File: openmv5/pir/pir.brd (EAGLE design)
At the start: 35.6 x 26.7 mm, 60 parts, among them IC1 AP3032KTR-G1, IC2 AP3032KTR-G1, J1 OPENMV5-TOP, Q1 2N7002KW_R1_00001, U1 EKMB1307113K, U2 MIC5365-3.3YMT-TZ

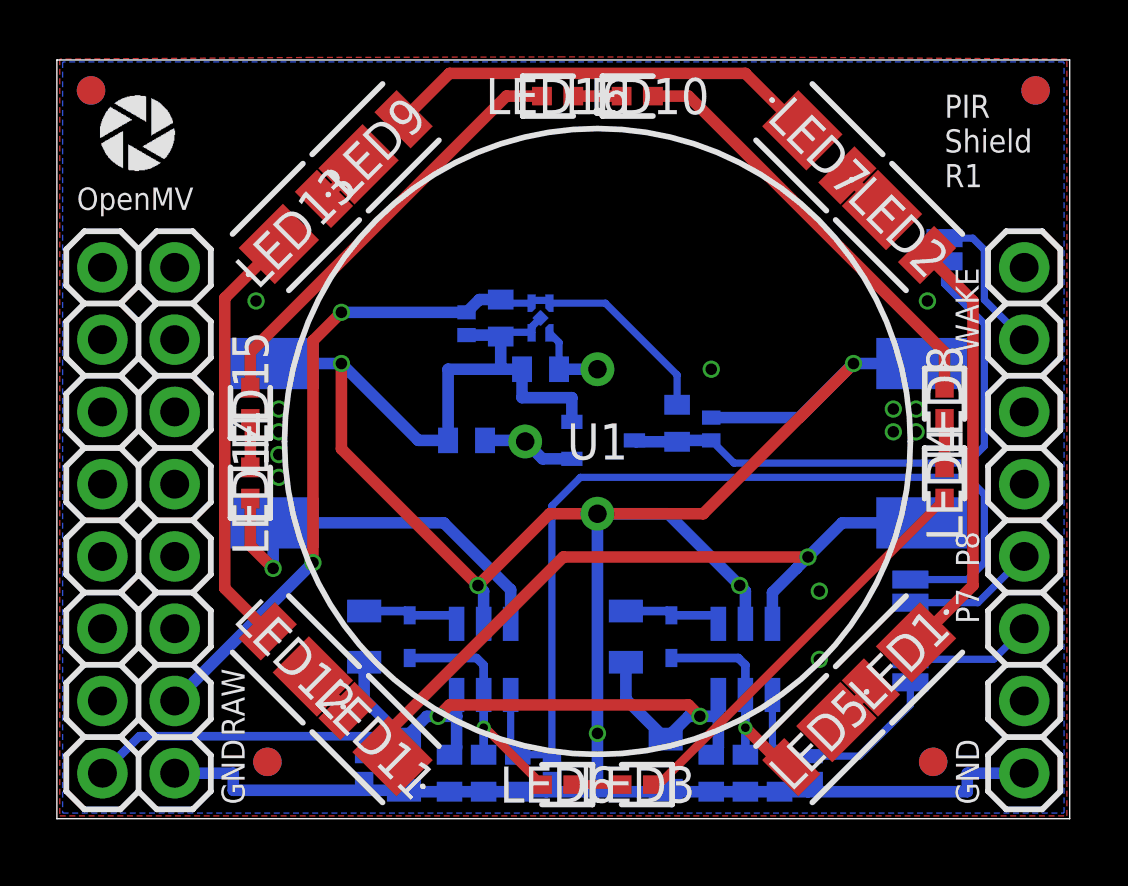
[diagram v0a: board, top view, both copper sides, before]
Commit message: Final PIR shield, fixed regulator
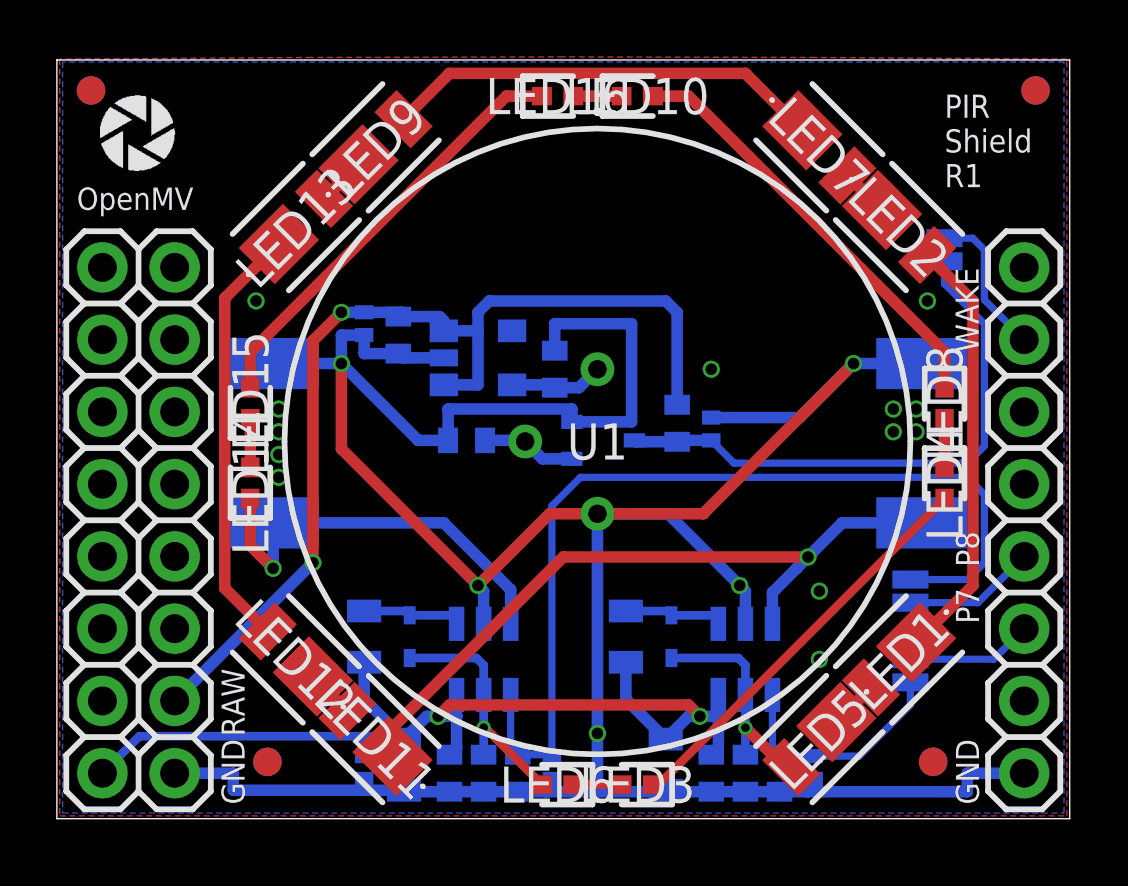
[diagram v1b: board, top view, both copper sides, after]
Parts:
- removed U2: MIC5365-3.3YMT-TZ, MIC5365-3.3YMT-TZ:VREG_MIC5365-3.3YMT-TZ
- added IC3: TCR2LF33,LM_CT, TCR2LF33_LM_CT:TCR2LF33LMCT
- moved C7 3.65 mm to (12.0, 17.0)
- moved D7 3.60 mm to (10.8, 17.4)
- moved C8 0.50 mm to (17.5, 15.8), turned to 270 degrees
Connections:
- net GND: now also IC3.2; no longer U2.2, U2.EP
- net RAW: now also IC3.1, IC3.3; no longer U2.3, U2.4
- net VDD: now also IC3.5; no longer U2.1
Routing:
- net GND: track 106.1 -> 113.9 mm
- net RAW: track 30.4 -> 36.2 mm
- net VDD: track 2.77 -> 3.31 mm

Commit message: Add more options
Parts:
- added JP4: JUMPER-SMT_2_NO_SILK, SparkFun-Jumpers:SMT-JUMPER_2_NO_SILK
- R5: value 1K -> 100K
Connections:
- new net P11_WAKEUP_INT_2: J1.13, JP4.1
- net P11_WAKEUP: now also JP4.2
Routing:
- net P11_WAKEUP_INT_2: track 0.00 -> 22.5 mm, vias 0 -> 2
- net GND: track 113.9 -> 115.0 mm
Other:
- board text added: "WAKE P11"
- board text added: "WAKE P9"
- board text removed: "WAKE"
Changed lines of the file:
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@@
 <wire x1="35.6" y1="26.67" x2="0" y2="26.67" width="0" layer="20"/>
 <wire x1="0" y1="26.67" x2="0" y2="0" width="0" layer="20"/>
-<text x="24.4" y="19" size="0.8128" layer="22" font="vector" ratio="20" rot="MR0">https://openmv.io</text>
+<text x="23.2" y="19" size="0.8128" layer="22" font="vector" ratio="20" rot="MR0">https://openmv.io</text>
 <text x="0.7" y="21.4" size="0.7874" layer="21" font="vector" ratio="20" distance="30">OpenMV</text>
-<text x="24.4" y="20.4" size="0.8128" layer="22" font="vector" ratio="20" rot="MR0">PIR Shield R1</text>
-<text x="24.4" y="17.6" size="0.8128" layer="22" font="vector" ratio="20" rot="MR0">3.31.23</text>
+<text x="23.2" y="20.4" size="0.8128" layer="22" font="vector" ratio="20" rot="MR0">PIR Shield R1</text>
+<text x="23.2" y="17.6" size="0.8128" layer="22" font="vector" ratio="20" rot="MR0">3.31.23</text>
 <text x="5.8" y="0.5" size="0.8128" layer="22" font="vector" ratio="22" rot="MR90">GND</text>
 <text x="32.4" y="2.8" size="0.8128" layer="22" font="vector" ratio="22" rot="MR270">GND</text>
@@
 <text x="6.6" y="2.9" size="0.8128" layer="21" font="vector" ratio="22" rot="R90">RAW</text>
 <text x="31.6" y="2.8" size="0.8128" layer="21" font="vector" ratio="22" rot="R270">GND</text>
-<text x="31.6" y="8.1" size="0.8128" layer="21" font="vector" ratio="22" rot="R270">P7</text>
-<text x="31.6" y="10.1" size="0.8128" layer="21" font="vector" ratio="22" rot="R270">P8</text>
-<text x="32.4" y="16.4" size="0.8128" layer="21" font="vector" ratio="22" rot="R90">WAKE</text>
 <text x="10.8" y="14" size="0.8128" layer="22" font="vector" ratio="20" rot="MR270">Hot</text>
 <text x="27.2" y="12" size="0.8128" layer="22" font="vector" ratio="20" rot="MR90">Hot</text>
 <text x="28.6" y="6" size="0.8128" layer="22" font="vector" ratio="22" rot="MR270">P7</text>
 <text x="28.6" y="8.8" size="0.8128" layer="22" font="vector" ratio="22" rot="MR270">P8</text>
-<text x="29.9" y="21.5" size="0.8128" layer="22" font="vector" ratio="22" rot="MR270">WAKE</text>
+<text x="29.9" y="21.5" size="0.8128" layer="22" font="vector" ratio="22" rot="MR270">WAKE
+P11</text>
 <text x="5.8" y="2.9" size="0.8128" layer="22" font="vector" ratio="22" rot="MR90">RAW</text>
+<text x="27.1" y="15.9" size="0.8128" layer="22" font="vector" ratio="22" rot="MR0">WAKE
+P9</text>
 </plain>
 <attributes>
@@
 <attribute name="VALUE" x="10.857" y="15.9205" size="0.4064" layer="28" rot="MR90"/>
 </element>
-<element name="R5" library="sfe" package="0402-RES" value="1K" x="21.8" y="13.9" smashed="yes" rot="MR90">
-<attribute name="MPN" value="CRCW04021K00FKEDC" x="25" y="10.7" size="1.778" layer="28" rot="MR90" display="off"/>
+<element name="R5" library="sfe" package="0402-RES" value="100K" x="21.8" y="13.9" smashed="yes" rot="MR90">
+<attribute name="MPN" value="AC0402FR-07100KL" x="25" y="10.7" size="1.778" layer="28" rot="MR90" display="off"/>
 <attribute name="NAME" x="22.4985" y="13.011" size="0.4064" layer="26" rot="MR90"/>
 <attribute name="VALUE" x="20.657" y="12.8205" size="0.4064" layer="28" rot="MR90"/>
@@
 <attribute name="NAME" x="14.8" y="16.2" size="1.27" layer="26" rot="MR90" align="center"/>
 <attribute name="VALUE" x="14.8" y="16.2" size="1.27" layer="28" rot="MR90" align="center"/>
+</element>
+<element name="JP4" library="SparkFun-Jumpers" library_urn="urn:adsk.eagle:library:528" package="SMT-JUMPER_2_NO_SILK" package3d_urn="urn:adsk.eagle:package:39279/1" value="JUMPER-SMT_2_NO_SILK" x="25.6" y="14.4" smashed="yes" rot="MR270">
+<attribute name="NAME" x="24.457" y="14.4" size="0.6096" layer="26" font="vector" ratio="20" rot="MR270" align="bottom-center"/>
+<attribute name="VALUE" x="26.743" y="14.4" size="0.6096" layer="28" font="vector" ratio="20" rot="MR270" align="top-center"/>
 </element>
 </elements>
@@
 <wire x1="13.75" y1="13.3" x2="12.7" y2="13.3" width="0.4064" layer="16"/>
 <wire x1="12.7" y1="13.3" x2="10" y2="16" width="0.4064" layer="16"/>
-<wire x1="28" y1="16" x2="26.1" y2="14.1" width="0.4064" layer="16"/>
-<wire x1="26.1" y1="14.1" x2="23" y2="14.1" width="0.4064" layer="16"/>
 <wire x1="12" y1="16.35" x2="11.95" y2="16.4" width="0.4064" layer="16"/>
 <wire x1="12" y1="16.35" x2="12.15" y2="16.5" width="0.254" layer="16"/>
@@
 <via x="29.4" y="13.6" extent="1-16" drill="0.4064"/>
 <via x="29.4" y="14.4" extent="1-16" drill="0.4064"/>
-<via x="23" y="15.8" extent="1-16" drill="0.4064"/>
+<via x="23" y="16" extent="1-16" drill="0.4064"/>
 <contactref element="IC3" pad="2"/>
 <wire x1="13.6" y1="16.2" x2="12.15" y2="16.2" width="0.4064" layer="16"/>
@@
 <wire x1="18.1" y1="14.4" x2="18.1" y2="13.95" width="0.4064" layer="16"/>
 <wire x1="13.75" y1="14.4" x2="18.1" y2="14.4" width="0.4064" layer="16"/>
+<wire x1="23" y1="14.1" x2="23" y2="16" width="0.4064" layer="16"/>
+<wire x1="23" y1="16" x2="28" y2="16" width="0.4064" layer="16"/>
 </signal>
 <signal name="N$69">
@@
 <wire x1="23" y1="13.3" x2="21.85" y2="13.3" width="0.4064" layer="16"/>
 <wire x1="21.85" y1="13.3" x2="21.8" y2="13.25" width="0.4064" layer="16"/>
-<wire x1="32" y1="12.5" x2="23.8" y2="12.5" width="0.254" layer="16"/>
-<wire x1="23.8" y1="12.5" x2="23" y2="13.3" width="0.254" layer="16"/>
-<wire x1="32" y1="12.5" x2="32.6" y2="13.1" width="0.254" layer="16"/>
+<wire x1="32" y1="13" x2="25.6" y2="13" width="0.254" layer="16"/>
+<wire x1="25.6" y1="13" x2="23.3" y2="13" width="0.254" layer="16"/>
+<wire x1="23.3" y1="13" x2="23" y2="13.3" width="0.254" layer="16"/>
+<wire x1="32" y1="13" x2="32.6" y2="13.6" width="0.254" layer="16"/>
 <contactref element="JP3" pad="2"/>
-<wire x1="32.6" y1="13.1" x2="32.6" y2="17.4" width="0.254" layer="16"/>
+<wire x1="32.6" y1="13.6" x2="32.6" y2="17.4" width="0.254" layer="16"/>
 <wire x1="32.6" y1="17.4" x2="31.2" y2="18.8" width="0.254" layer="16"/>
 <wire x1="31.2" y1="19.5936" x2="31.2" y2="18.8" width="0.254" layer="16"/>
+<contactref element="JP4" pad="2"/>
+<wire x1="25.6" y1="13.9936" x2="25.6" y2="13" width="0.254" layer="16"/>
 </signal>
 <signal name="P7_PWM" class="4">
@@
 <wire x1="32.6" y1="20" x2="32.6" y2="18.24" width="0.254" layer="16"/>
 </signal>
+<signal name="P11_WAKEUP_INT_2" class="4">
+<contactref element="J1" pad="13"/>
+<contactref element="JP4" pad="1"/>
+<wire x1="34" y1="11.76" x2="33.26" y2="12.5" width="0.254" layer="16"/>
+<wire x1="19.7" y1="12.5" x2="19.2" y2="13" width="0.254" layer="16"/>
+<via x="19.2" y="13" extent="1-16" drill="0.254"/>
+<wire x1="33.26" y1="12.5" x2="19.7" y2="12.5" width="0.254" layer="16"/>
+<wire x1="25.6" y1="14.8064" x2="25.5936" y2="14.8" width="0.254" layer="16"/>
+<wire x1="25.5936" y1="14.8" x2="24" y2="14.8" width="0.254" layer="16"/>
+<via x="24" y="14.8" extent="1-16" drill="0.254"/>
+<wire x1="24" y1="14.8" x2="22.2" y2="13" width="0.254" layer="1"/>
+<wire x1="22.2" y1="13" x2="19.2" y2="13" width="0.254" layer="1"/>
+</signal>
 </signals>
